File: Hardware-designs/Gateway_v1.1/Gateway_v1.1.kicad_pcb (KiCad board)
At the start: 2 copper layers, 74.2 x 74.2 mm, 39 parts, among them J1 UART, J3 USB_C, J4 UART, SW1 main, SW2 Aux, U1 ESP32-TCP, U2 AMS1117, U3 AMS1117, U4 ESP32-NOW

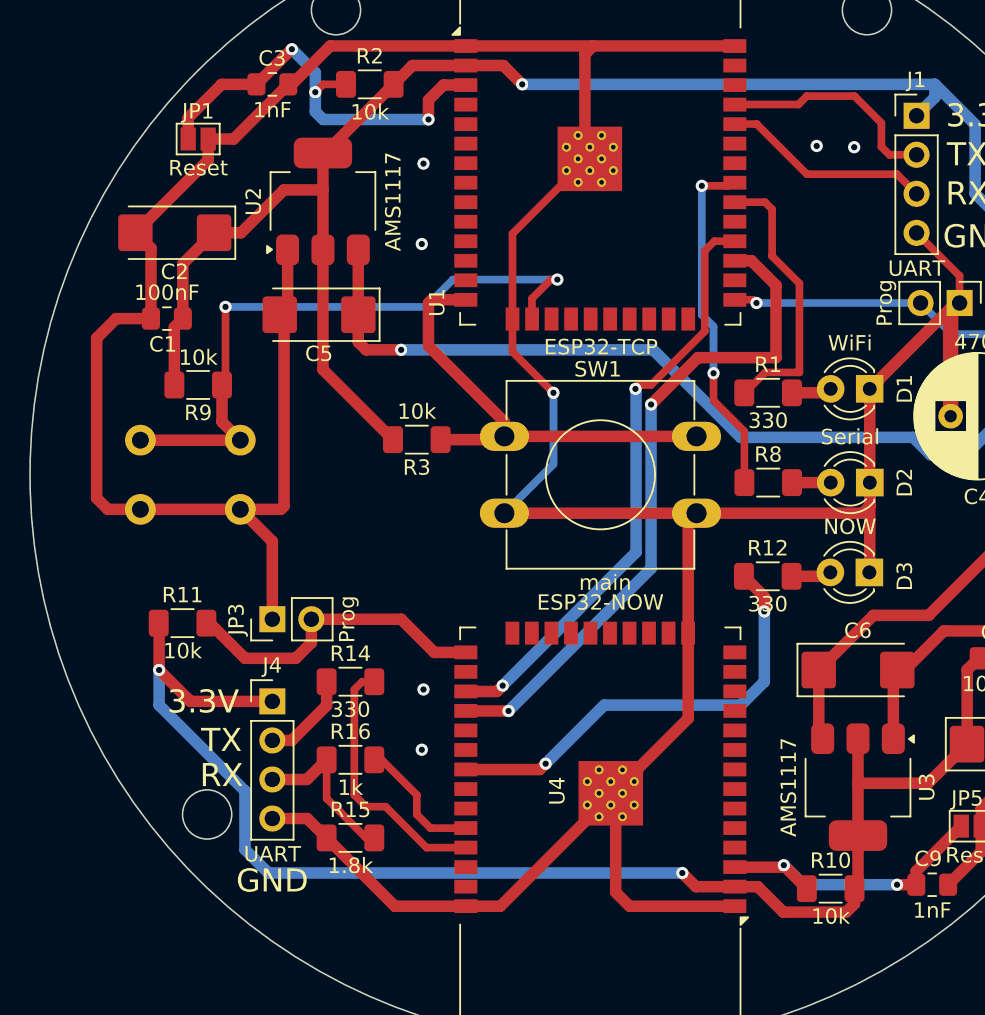
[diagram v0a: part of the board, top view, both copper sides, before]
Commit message: Add pcb images, step file, and pdf schematic for all hardware designs.
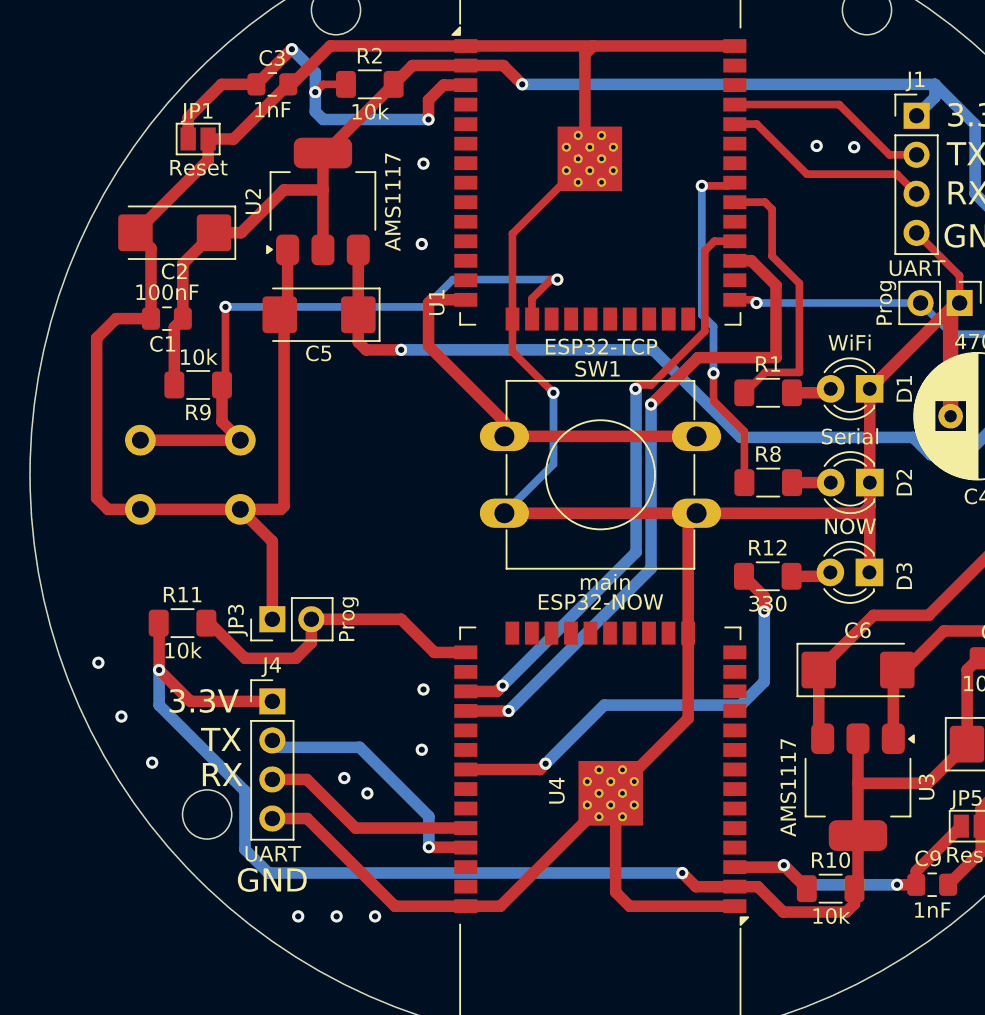
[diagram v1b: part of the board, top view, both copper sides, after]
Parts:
- removed R14: 330, Resistor_SMD:R_1206_3216Metric_Pad1.30x1.75mm_HandSolder
- removed R15: 1.8k, Resistor_SMD:R_1206_3216Metric_Pad1.30x1.75mm_HandSolder
- removed R16: 1k, Resistor_SMD:R_1206_3216Metric_Pad1.30x1.75mm_HandSolder
- removed R3: 10k, Resistor_SMD:R_1206_3216Metric_Pad1.30x1.75mm_HandSolder
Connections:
- U4 pad 34: Net-(U4-RXD0/IO3) -> Net-(J4-Pin_3)
- U4 pad 35: Net-(U4-TXD0/IO1) -> Net-(J4-Pin_2)
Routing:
- net Net-(U4-TXD0/IO1): track 17.3 -> 0.00 mm
- net +3.3V: track 102.0 -> 87.7 mm
- net Net-(J4-Pin_2): track 6.02 -> 16.6 mm, vias 0 -> 1
- net Net-(U4-RXD0/IO3): track 8.79 -> 0.00 mm
- net Net-(U1-IO12): track 30.2 -> 26.3 mm
- net Net-(J4-Pin_3): track 10.7 -> 13.9 mm
- net Net-(J1-Pin_2): track 14.8 -> 13.4 mm
- net GND: vias 7 -> 15

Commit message: Minor KiCad files update for all devices
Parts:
- C3, C9: value 1nF -> 68nF
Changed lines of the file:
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@@
 			)
 		)
-		(property "Value" "1nF"
+		(property "Value" "68nF"
 			(at 0 1.68 0)
 			(layer "F.SilkS")
@@
 			)
 		)
-		(property "Value" "1nF"
+		(property "Value" "68nF"
 			(at 0 1.68 0)
 			(layer "F.SilkS")
